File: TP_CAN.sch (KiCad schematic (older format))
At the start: 1 part, among them J13 4p Terminal Block

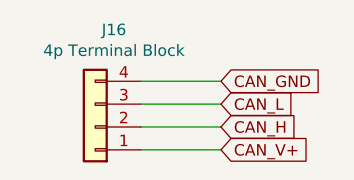
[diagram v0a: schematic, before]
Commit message: Add protection TVS and GDT. Rename TP file.
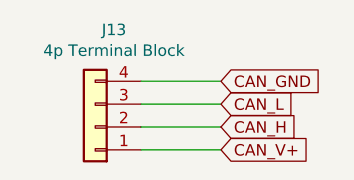
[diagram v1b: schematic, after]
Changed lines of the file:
@@
 Sheet 16 16
 Title "CAN Distributor"
-Date "2021-04-03"
-Rev "2.0"
+Date "2021-04-04"
+Rev "2.1"
 Comp ""
 Comment1 "Designed by: Erik Almbratt"
@@
 AR Path="/606A6FCD/606A774B" Ref="J15"  Part="1"
 AR Path="/606A70AE/606A774B" Ref="J16"  Part="1"
-F 0 "J16" H 5218 3175 50  0000 C CNN
+F 0 "J13" H 5218 3175 50  0000 C CNN
 F 1 "4p Terminal Block" H 5218 3266 50  0000 C CNN
 F 2 "TerminalBlock_TE-Connectivity:TerminalBlock_TE_282834-4_1x04_P2.54mm_Horizontal" H 5300 3600 50  0001 C CNN
